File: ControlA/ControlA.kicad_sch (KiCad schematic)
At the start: 0 parts

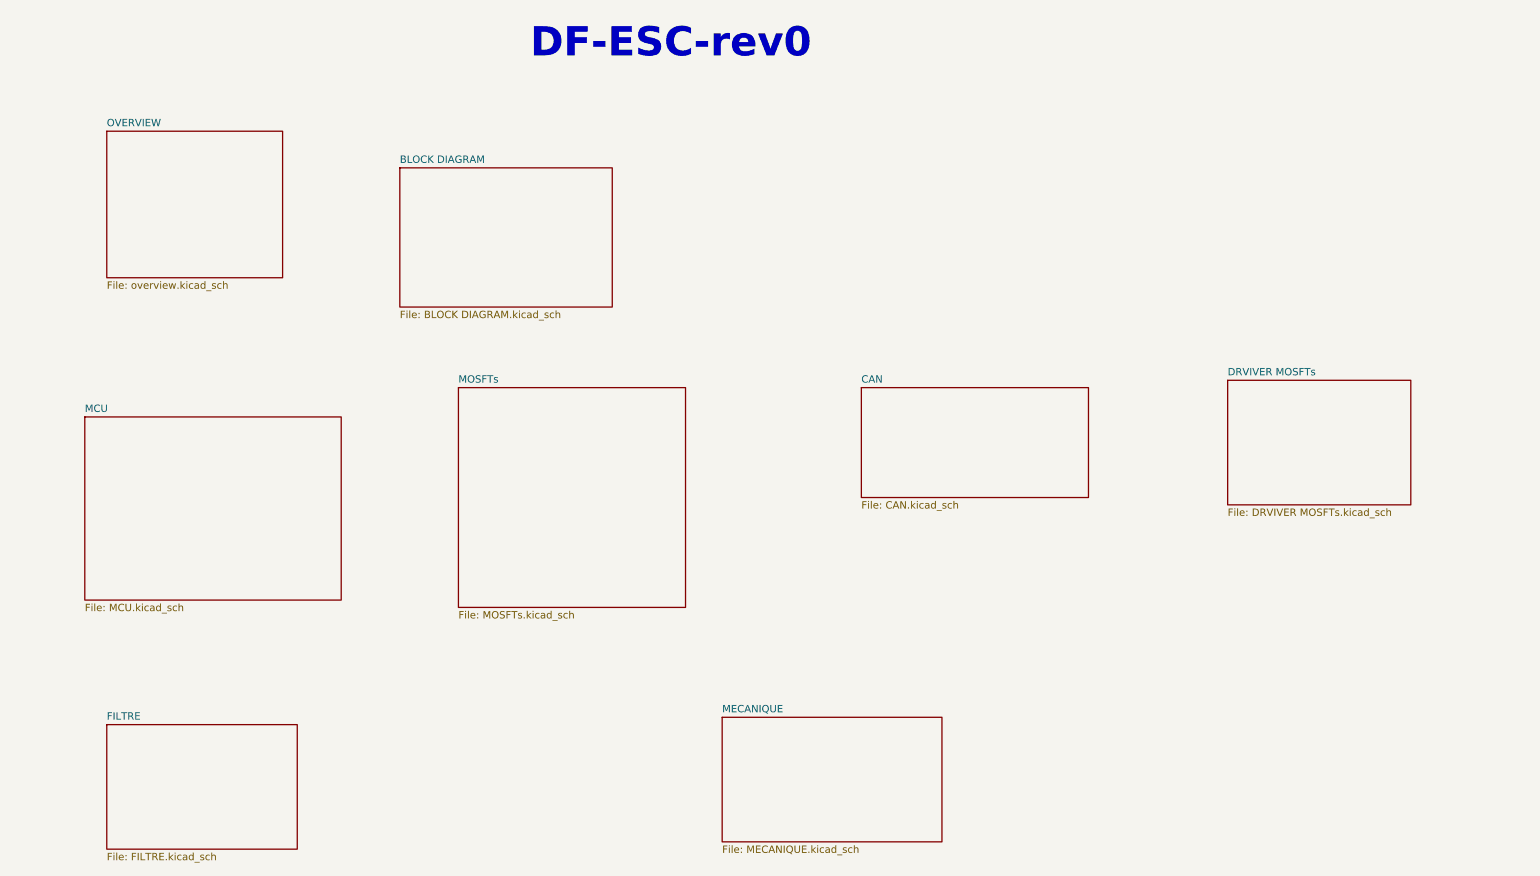
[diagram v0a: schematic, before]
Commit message: add libray symbole and add sheet
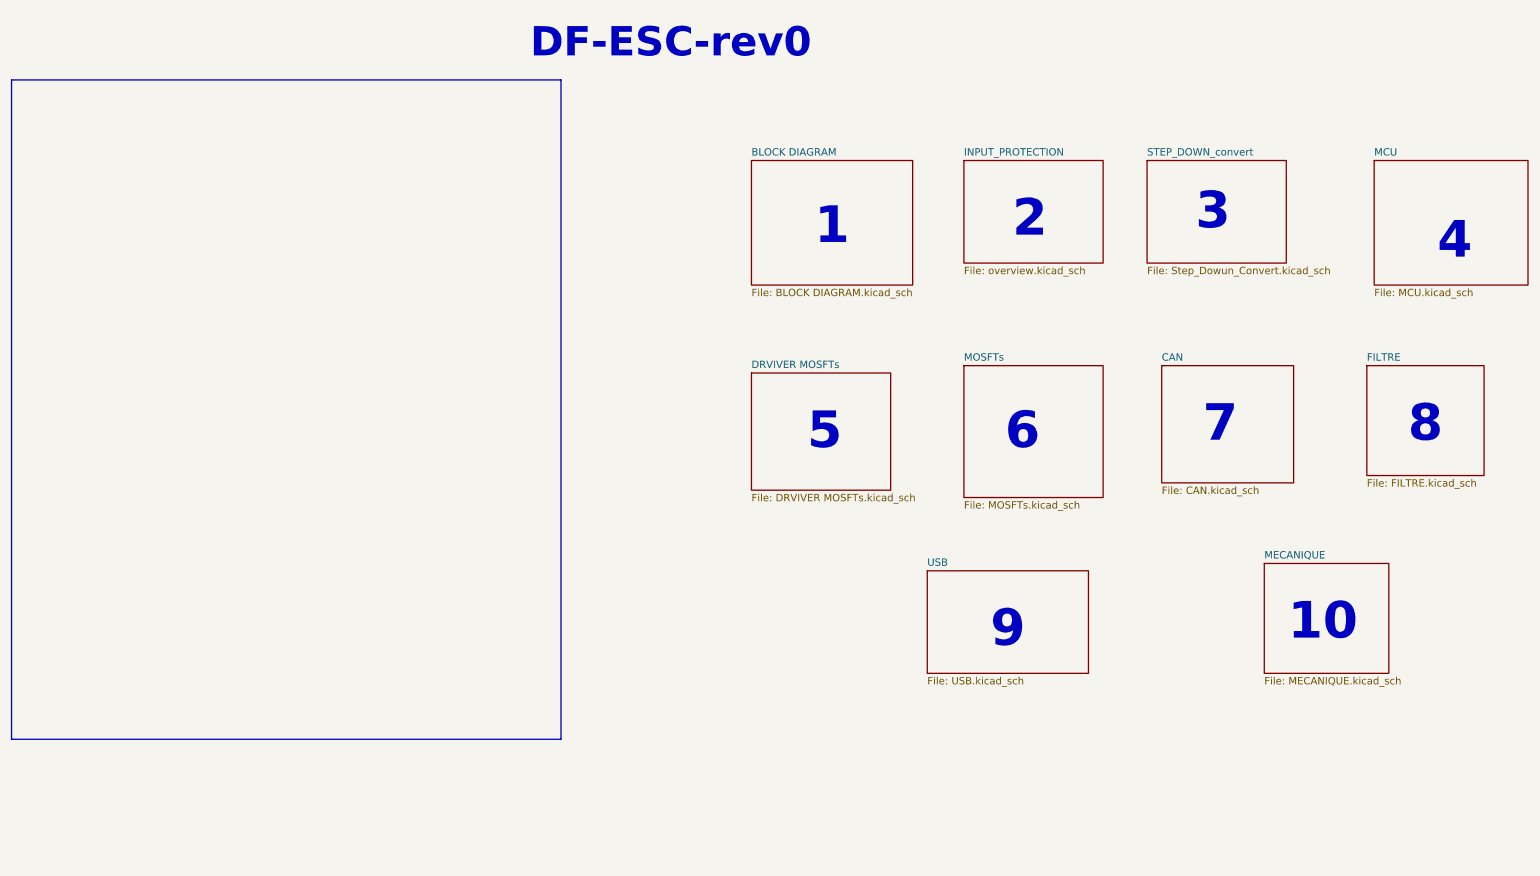
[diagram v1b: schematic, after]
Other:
- sheet OVERVIEW renamed INPUT_PROTECTION
- added sheet STEP_DOWN_convert (Step_Dowun_Convert.kicad_sch)
- added sheet USB (USB.kicad_sch)
- note added: "1"
- note added: "10"
- note added: "2"
- note added: "3"
- note added: "4"
- note added: "5"
- note added: "6"
- note added: "7"
- note added: "8"
- note added: "9"
